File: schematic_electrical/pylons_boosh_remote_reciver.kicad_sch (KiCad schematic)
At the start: 0 parts

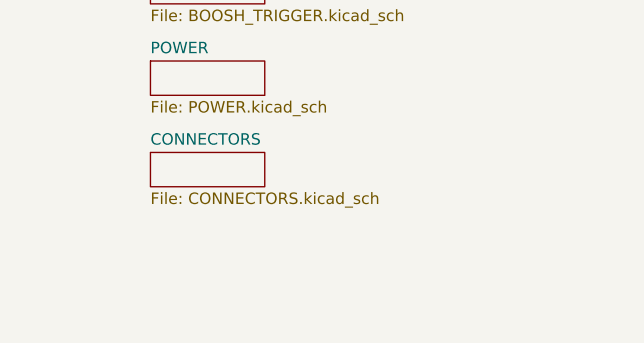
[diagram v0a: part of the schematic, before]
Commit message: Add expansion buttons/lamps schematic sheet; schematic cleanup and annotations
- New EXPANSION_BUTTONS_LAMPS.kicad_sch sheet wired into top-level schematic
- Add AB_800T-QT24 symbol library
- ESP32_MCU: wire previously unconnected GPIO pins to BUTTON0-4 and BUTTON_LAMP_PWM_OUT0-4 global labels; add expansion IO bounding box annotation
- POWER: add GND ganging fabrication notes, DCDC USB wiring note, fuse value updated to "10A MINI AUTO BLADE"; routing cleanup
- CONNECTORS: routing and junction cleanup
- BOOSH_TRIGGER: remove stale "1R" errata note
- IDEA.md: add sandbox notes and open questions

Co-Authored-By: Claude Sonnet 4.6 <noreply@anthropic.com>
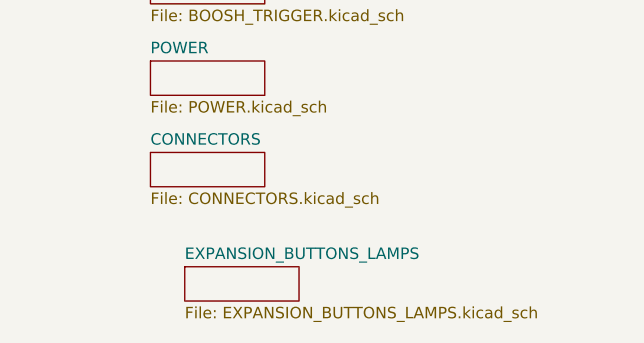
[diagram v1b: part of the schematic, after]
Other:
- added sheet EXPANSION_BUTTONS_LAMPS (EXPANSION_BUTTONS_LAMPS.kicad_sch)
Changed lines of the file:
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@@
+	)
+	(sheet
+		(at 48.26 93.98)
+		(size 12.7 3.81)
+		(fields_autoplaced yes)
+		(stroke
+			(width 0.1524)
+			(type solid)
+		)
+		(fill
+			(color 0 0 0 0.0000)
+		)
+		(property "Sheetname" "EXPANSION_BUTTONS_LAMPS"
+			(at 48.26 93.2684 0)
+			(effects
+				(font
+					(size 1.27 1.27)
+				)
+				(justify left bottom)
+			)
+		)
+		(property "Sheetfile" "EXPANSION_BUTTONS_LAMPS.kicad_sch"
+			(at 48.26 98.3746 0)
+			(effects
+				(font
+					(size 1.27 1.27)
+				)
+				(justify left top)
+			)
+		)
+		(instances
+			(project "pylons_boosh_remote_reciver"
+				(path "/f3653ac0-a28a-4ee8-bcf5-236139001455"
+					(page "6")
+				)
+			)
+		)
 	)
 	(sheet
